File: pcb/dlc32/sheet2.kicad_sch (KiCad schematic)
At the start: 29 parts, among them IC2 74HCT04, J10 VALVE/CHILLER SSR PWR, J11 EXHAUST, J14 EXT1, J15 COM2, J16 DLC32:J18, J17 EXT PWR, J4 CHILLER SWITCH, J5 CHILLER SSR, J6 AIR VALVE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

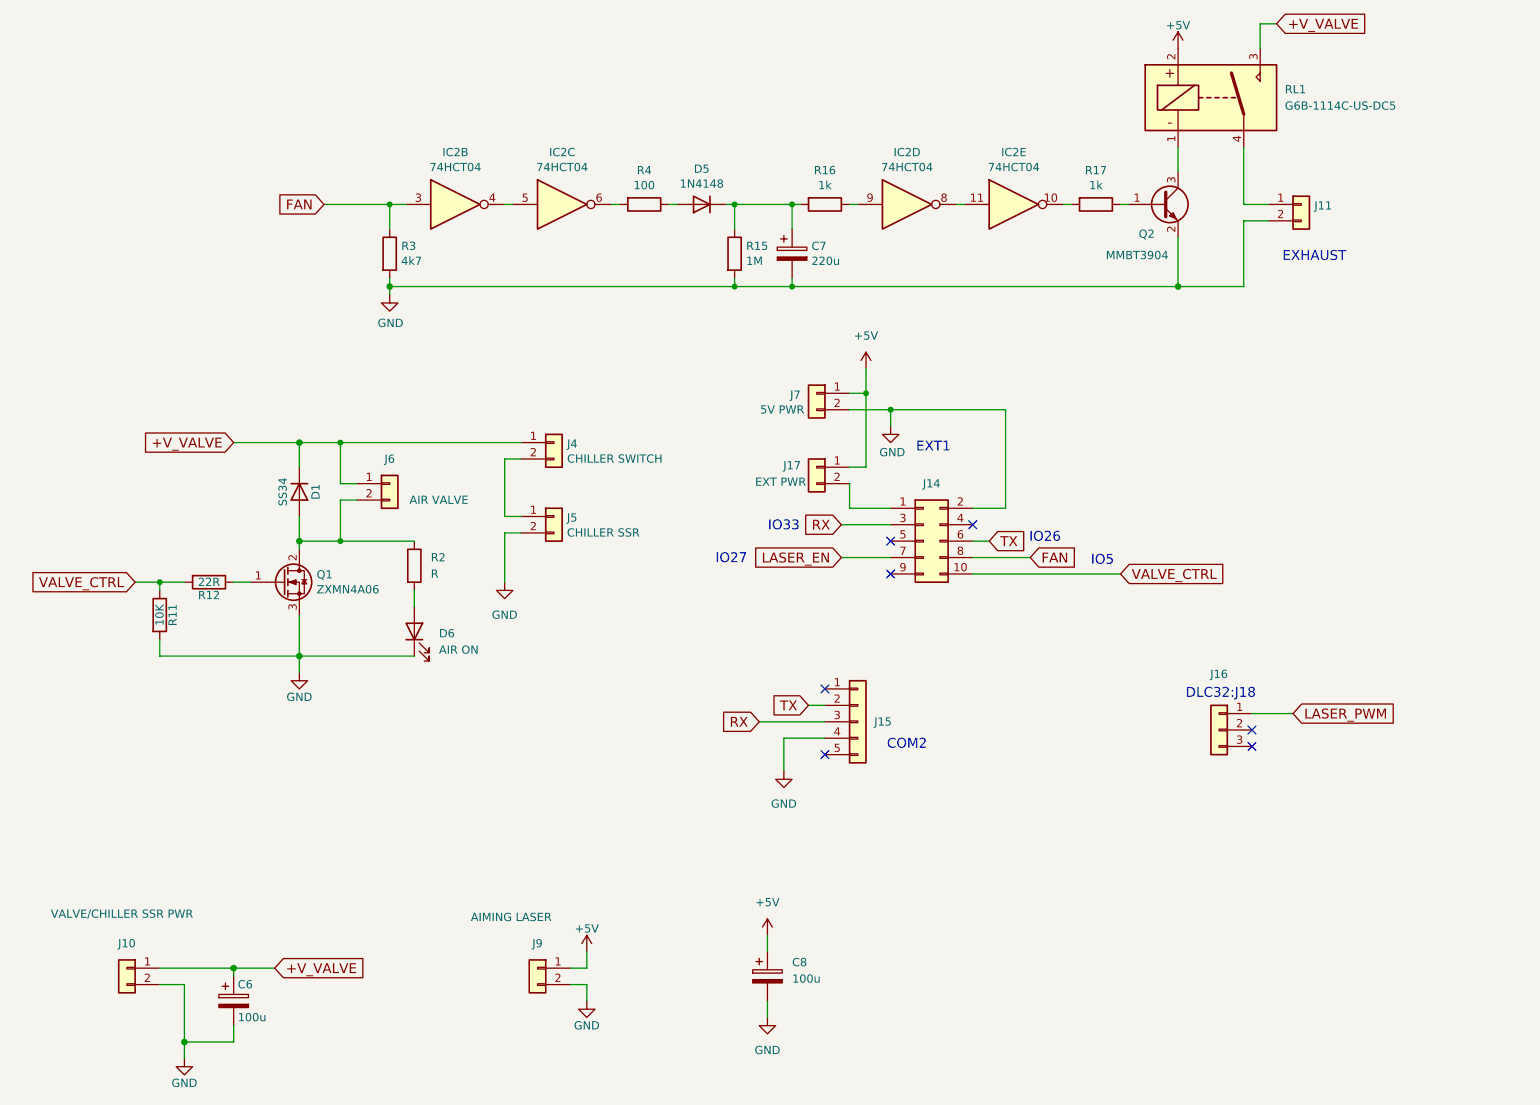
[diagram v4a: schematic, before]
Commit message: Use Schmitt triggers. Add clamping diodes, test point.
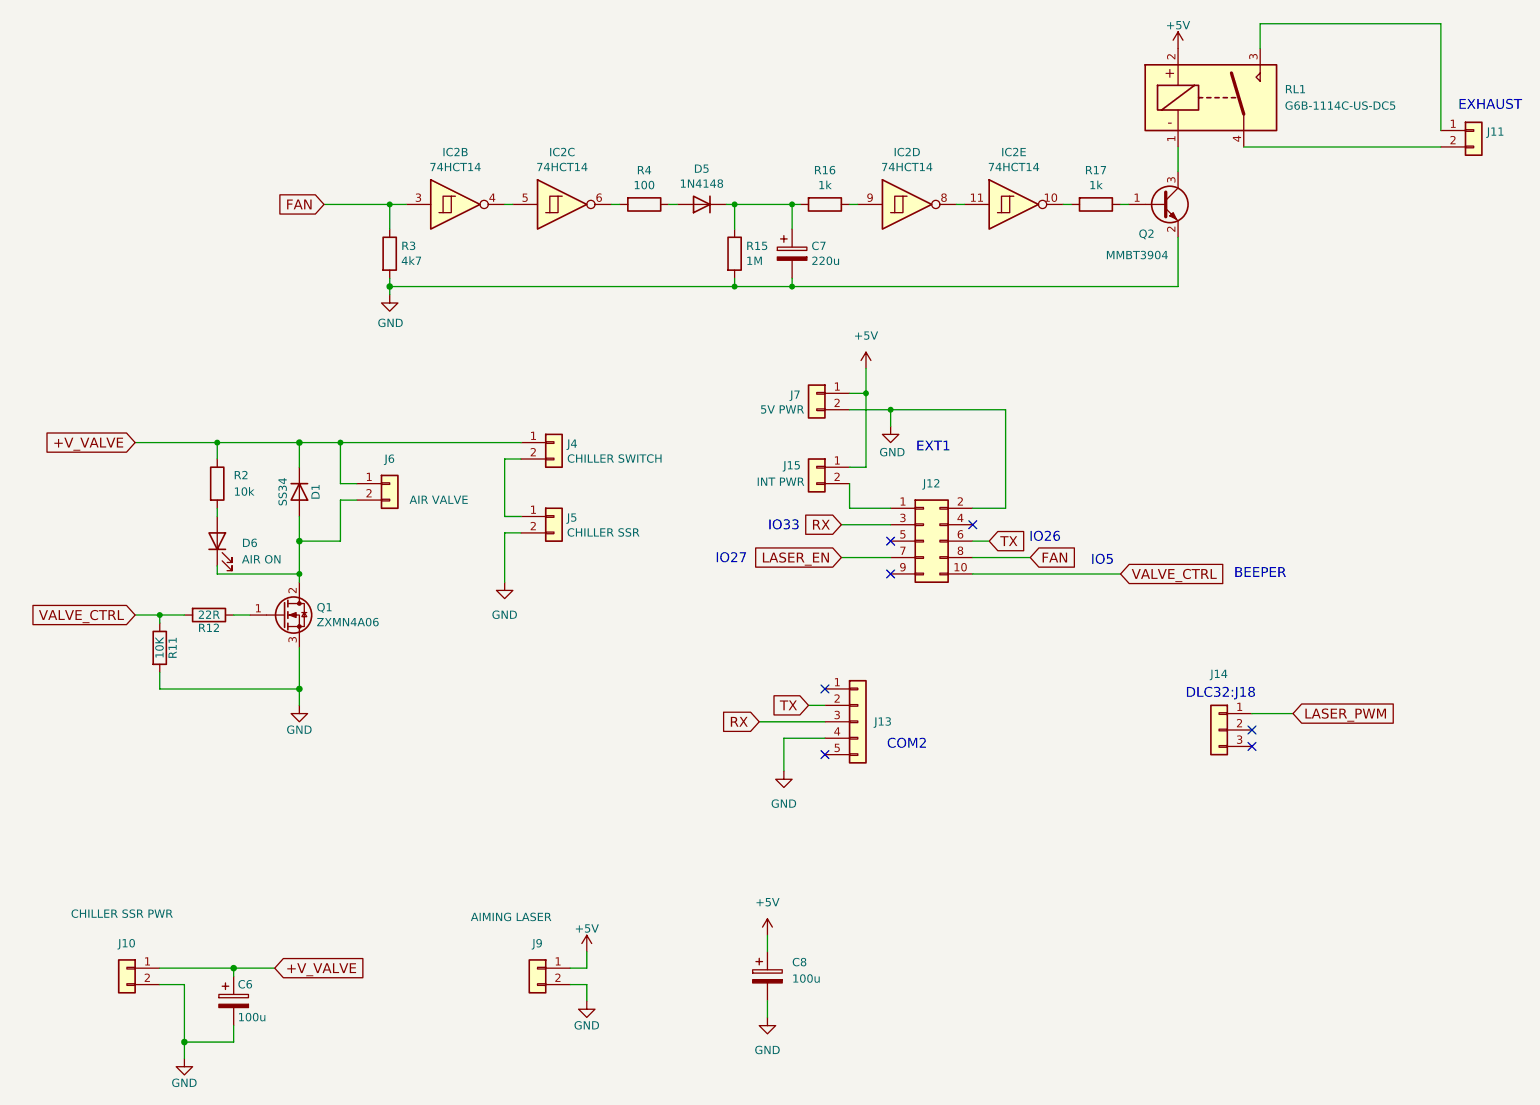
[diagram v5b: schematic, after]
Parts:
- D5: footprint Diode_SMD:D_MiniMELF -> PCM_Diode_SMD_AKL:D_MiniMELF
- IC2: value 74HCT04 -> 74HCT14; symbol 74xx:74HCT04 -> 74xx:74HC14
- J10: value VALVE/CHILLER SSR PWR -> CHILLER SSR PWR
- J15: renamed from J17; value EXT PWR -> INT PWR
- R2: value R -> 10k
- renumbered J14 to J12, J15 to J13, J16 to J14
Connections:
- net +V_VALVE: now also R2.1; no longer RL1.3
- net GND: no longer D6.1 (K), J11.2 (Pin_2)
- net at D1.2 (A), J6.2 (Pin_2), Q1.2 (D): now also D6.1 (K); no longer R2.1
- net at J11.1 (Pin_1): now also RL1.3; no longer RL1.4
- new net: J11.2 (Pin_2), RL1.4
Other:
- note added: "BEEPER"
- moved on the sheet: D6, J11, Q1, R11, R12, R2

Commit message: Change to tantalum cap. Optimize connector placement.
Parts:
- C7: footprint PCM_Capacitor_SMD_AKL:CP_Elec_10x10 -> PCM_Capacitor_Tantalum_SMD_AKL:CP_EIA-7343-15_Kemet-W
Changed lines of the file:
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@@
 			)
 		)
-		(property "Footprint" "PCM_Capacitor_SMD_AKL:CP_Elec_10x10"
+		(property "Footprint" "PCM_Capacitor_Tantalum_SMD_AKL:CP_EIA-7343-15_Kemet-W"
 			(at 139.3952 62.23 0)
 			(effects

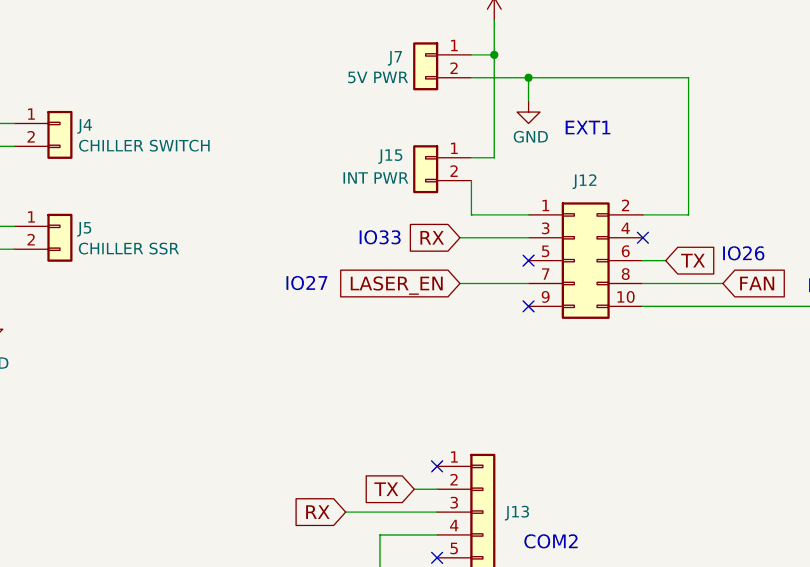
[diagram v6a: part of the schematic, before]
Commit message: Eliminate LASER_EN.
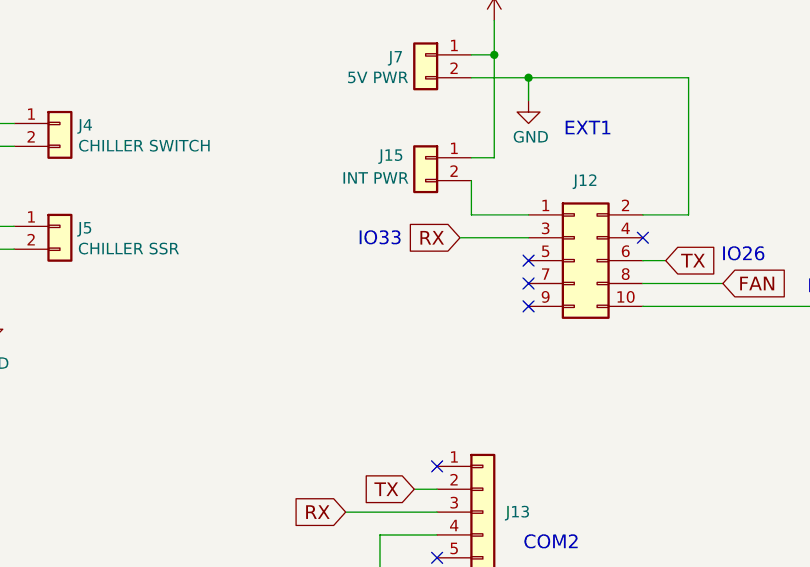
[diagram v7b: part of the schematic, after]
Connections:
- net LASER_EN: no longer names the net of J12.7 (Pin_7)
- no-connect marks 7 -> 8
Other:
- note removed: "IO27"
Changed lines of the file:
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@@
-		)
-	)
-	(text "IO27"
-		(exclude_from_sim no)
-		(at 129.032 105.664 0)
-		(effects
-			(font
-				(size 1.524 1.524)
-			)
 		)
 	)
@@
 	)
 	(no_connect
+		(at 153.67 105.41)
+	)
+	(no_connect
 		(at 209.55 132.08)
 	)
@@
 			(width 0)
 			(type solid)
-		)
-	)
-	(wire
-		(pts
-			(xy 146.05 105.41) (xy 153.67 105.41)
-		)
-		(stroke
-			(width 0)
-			(type default)
 		)
 	)
@@
 				(hide yes)
 			)
-		)
-	)
-	(global_label "LASER_EN"
-		(shape input)
-		(at 146.05 105.41 180)
-		(fields_autoplaced yes)
-		(effects
-			(font
-				(size 1.524 1.524)
-			)
-			(justify right)
-		)
-		(property "Intersheetrefs" "${INTERSHEET_REFS}"
-			(at 131.3231 105.41 0)
-			(effects
-				(font
-					(size 1.27 1.27)
-				)
-				(justify right)
-				(hide yes)
-			)

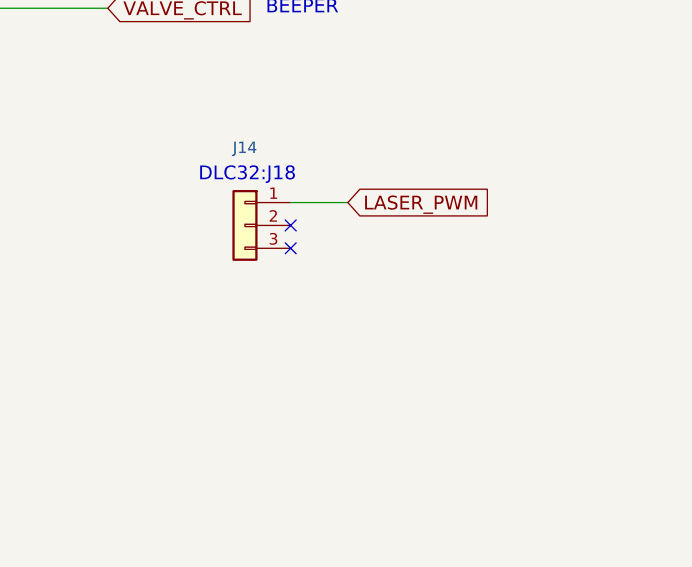
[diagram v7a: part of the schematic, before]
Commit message: Use correct pin on DLC32:J18.
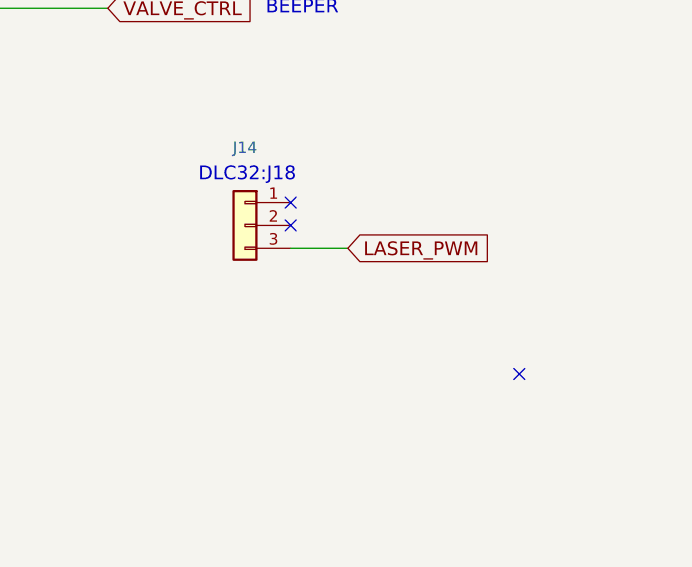
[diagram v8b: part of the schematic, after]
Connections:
- net LASER_PWM: now also J14.3 (Pin_3); no longer J14.1 (Pin_1)
- no-connect marks 8 -> 9
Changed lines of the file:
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@@
-	)
-	(no_connect
-		(at 209.55 134.62)
 	)
 	(no_connect
@@
 	)
 	(no_connect
+		(at 234.95 148.59)
+	)
+	(no_connect
+		(at 209.55 129.54)
+	)
+	(no_connect
 		(at 153.67 105.41)
 	)
@@
 	(wire
 		(pts
-			(xy 209.55 129.54) (xy 215.9 129.54)
-		)
-		(stroke
-			(width 0)
-			(type default)
-		)
-	)
-	(wire
-		(pts
 			(xy 140.97 128.27) (xy 143.51 128.27)
 		)
@@
 			(width 0)
 			(type solid)
+		)
+	)
+	(wire
+		(pts
+			(xy 209.55 134.62) (xy 215.9 134.62)
+		)
+		(stroke
+			(width 0)
+			(type default)
 		)
 	)
@@
 	(global_label "LASER_PWM"
 		(shape input)
-		(at 215.9 129.54 0)
+		(at 215.9 134.62 0)
 		(fields_autoplaced yes)
 		(effects
@@
 		)
 		(property "Intersheetrefs" "${INTERSHEET_REFS}"
-			(at 232.6588 129.54 0)
+			(at 232.6588 134.62 0)
 			(effects
 				(font
